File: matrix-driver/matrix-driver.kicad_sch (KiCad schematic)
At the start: 27 parts, among them J1 Conn_01x09, U1 TPS562202, U2 LP5891MRRFR, U3 TPS562202

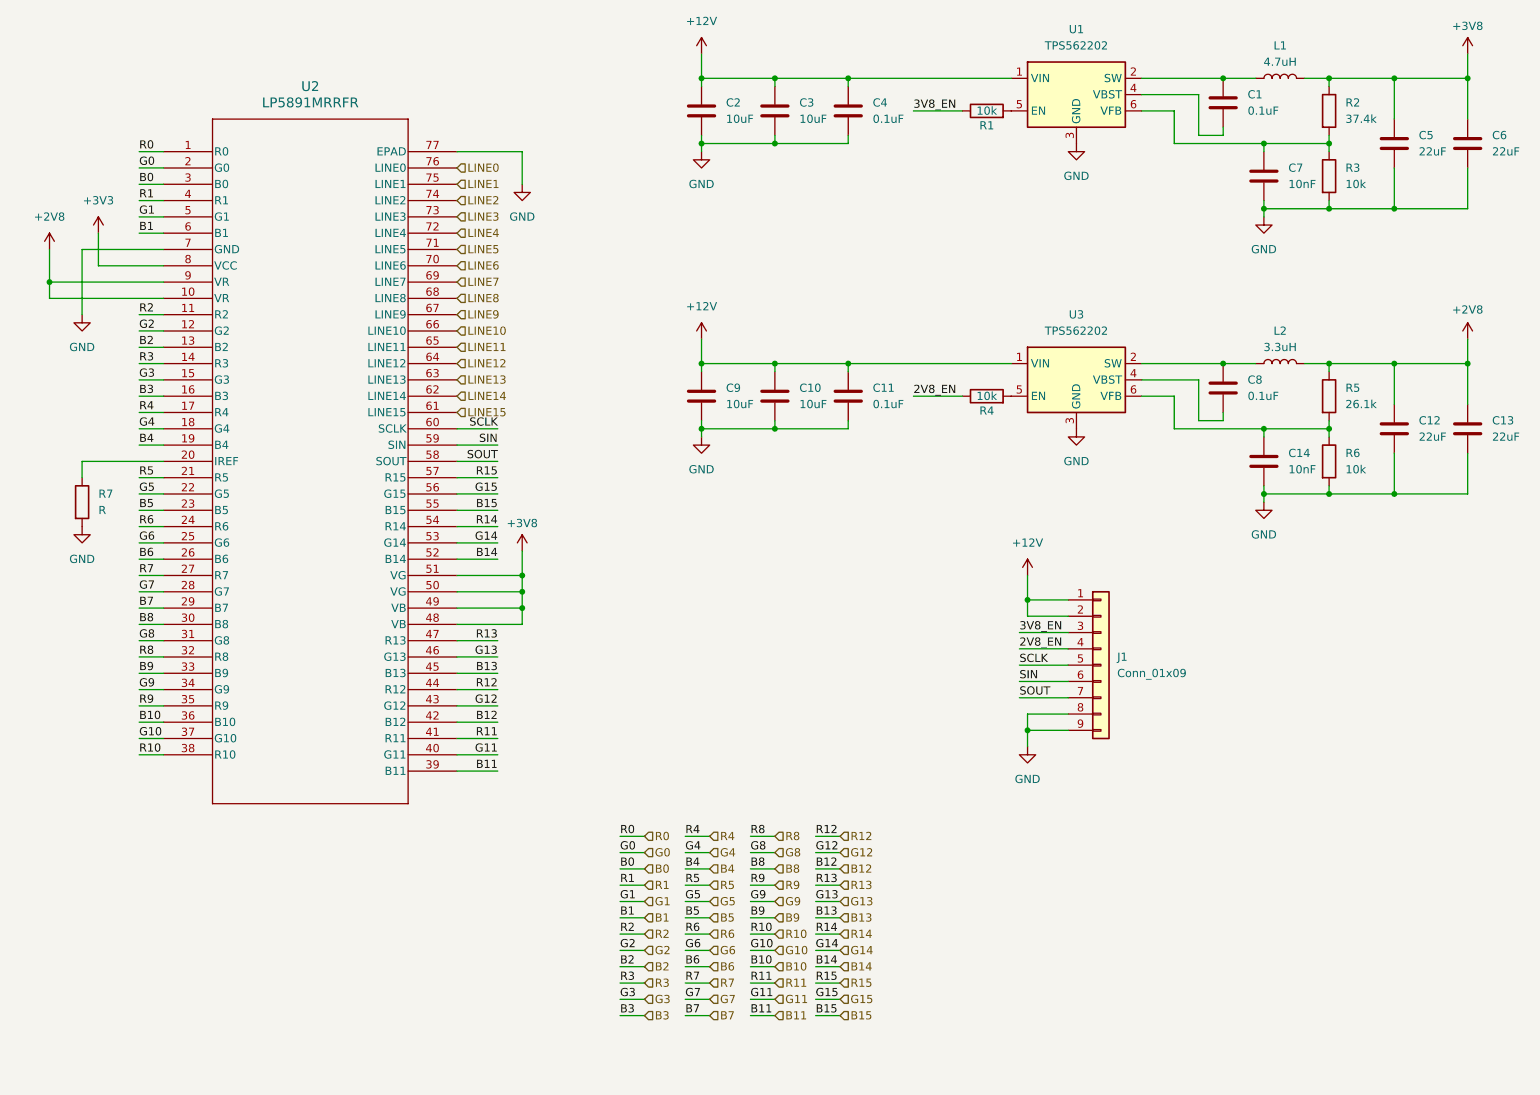
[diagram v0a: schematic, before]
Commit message: laid out proper schematic and connector interface for driver, added new conn libs, todo add correct inductors
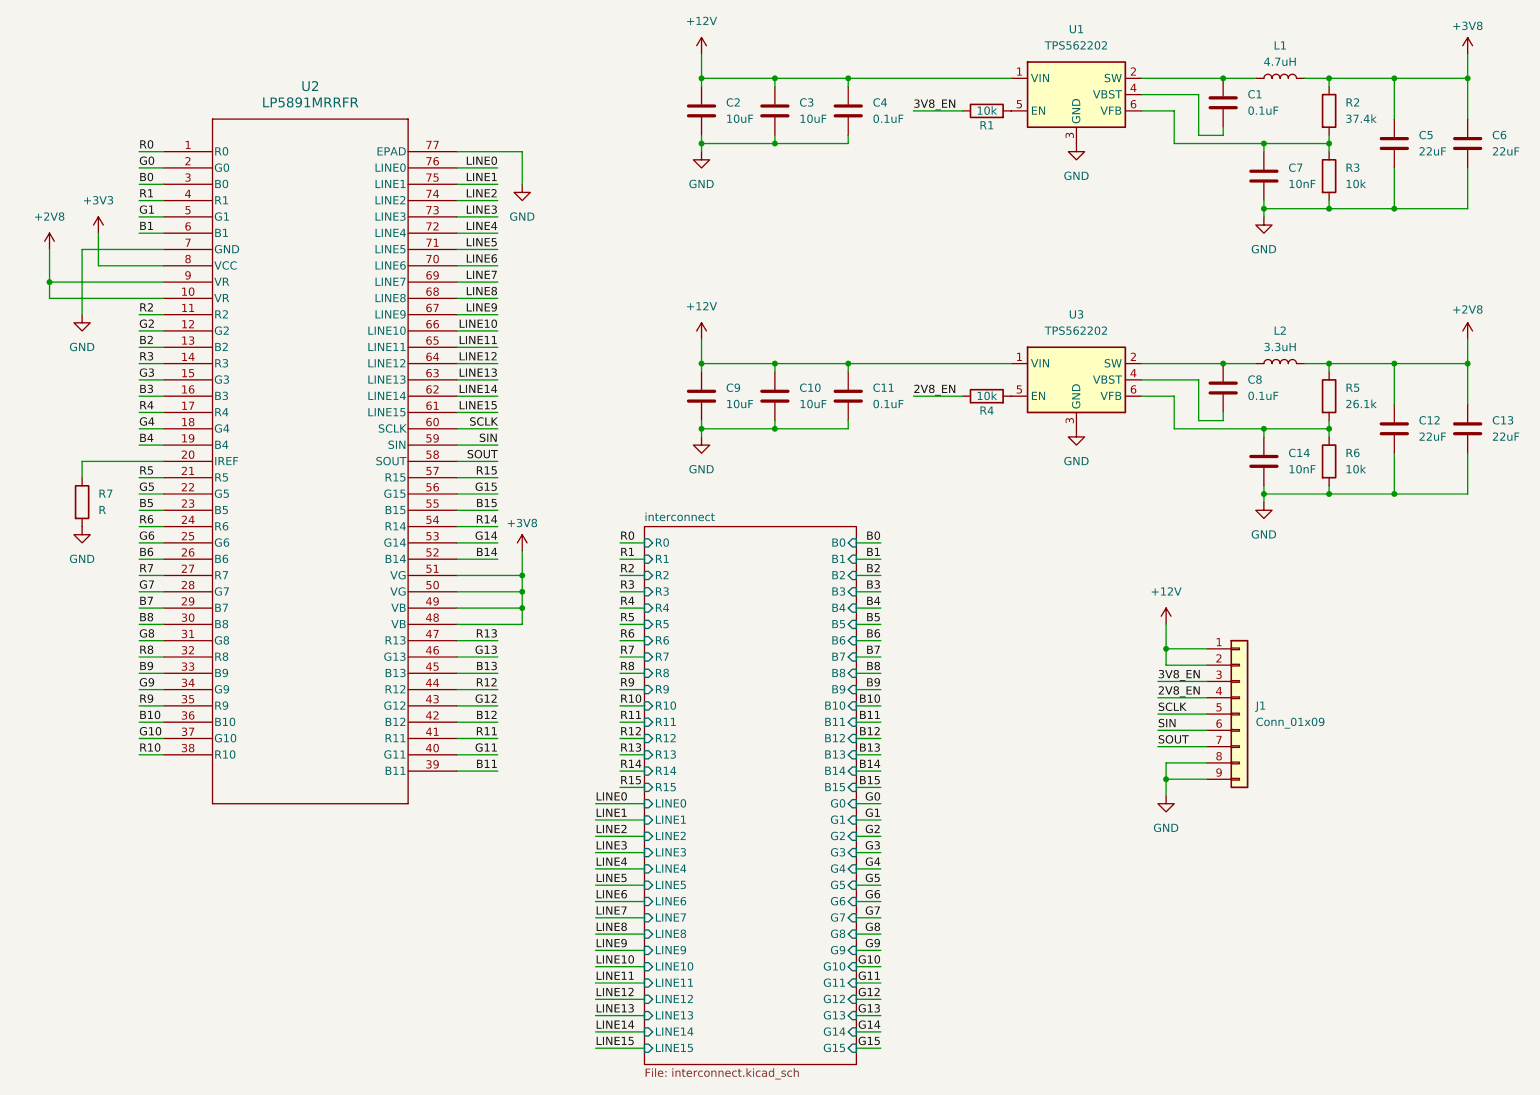
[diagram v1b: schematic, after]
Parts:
- J1: footprint (none) -> CONN_BM09B-XASS-TF_JST:CONN_BM09B-XASS-TF_JST
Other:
- added sheet interconnect (interconnect.kicad_sch)
- moved on the sheet: J1

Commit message: added 3v3 regulator again and added footprints to layout
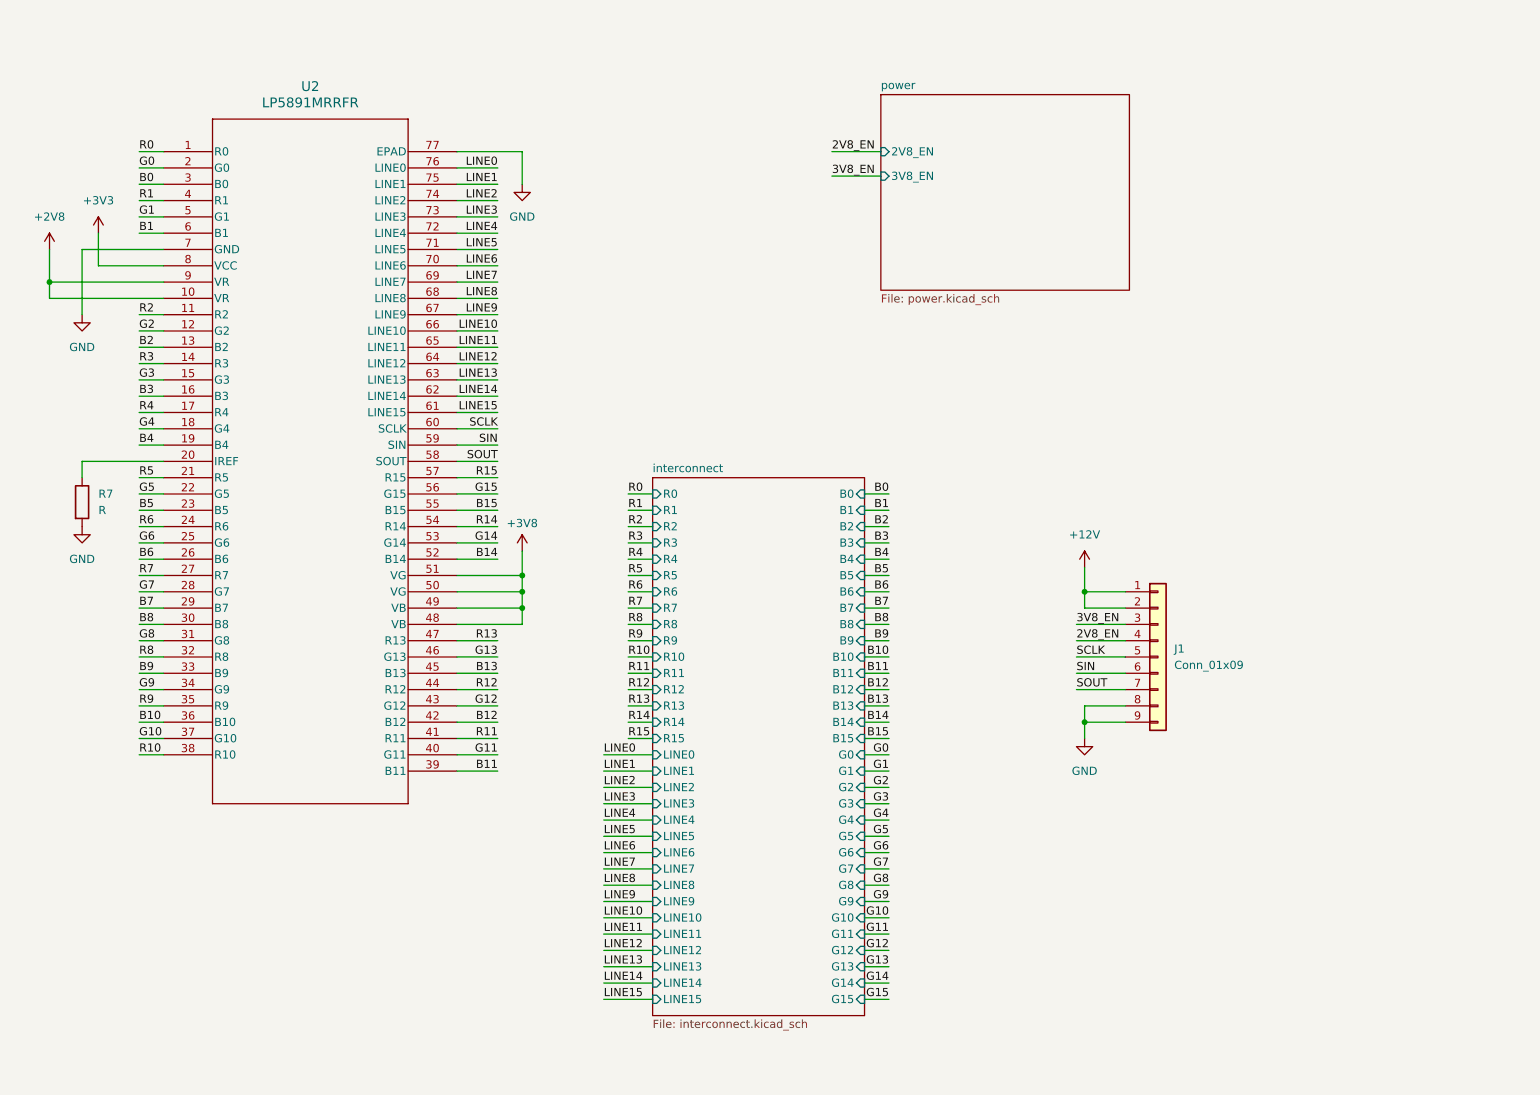
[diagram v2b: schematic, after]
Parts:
- removed C1, C11, C4, C8: 0.1uF, Capacitor_SMD:C_0603_1608Metric, symbol Device:C
- removed C10, C2, C3, C9: 10uF, Capacitor_SMD:C_1206_3216Metric, symbol Device:C
- removed C12, C13, C5, C6: 22uF, Capacitor_SMD:C_1206_3216Metric, symbol Device:C
- removed C14, C7: 10nF, Capacitor_SMD:C_0603_1608Metric, symbol Device:C
- removed L1: 4.7uH, symbol Device:L
- removed L2: 3.3uH, symbol Device:L
- removed R1, R3, R4, R6: 10k, Resistor_SMD:R_0603_1608Metric, symbol Device:R
- removed R2: 37.4k, Resistor_SMD:R_0603_1608Metric, symbol Device:R
- removed R5: 26.1k, Resistor_SMD:R_0603_1608Metric, symbol Device:R
- removed U1, U3: TPS562202, Package_TO_SOT_SMD:SOT-563, symbol Regulator_Switching:TPS562202
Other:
- added sheet power (power.kicad_sch)
- moved on the sheet: J1

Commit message: added gerbers and finalized v1.0
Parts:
- added H1, H2, H3, H4: MountingHole, MountingHole:MountingHole_3.2mm_M3_DIN965, symbol Mechanical:MountingHole
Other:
- moved on the sheet: J1

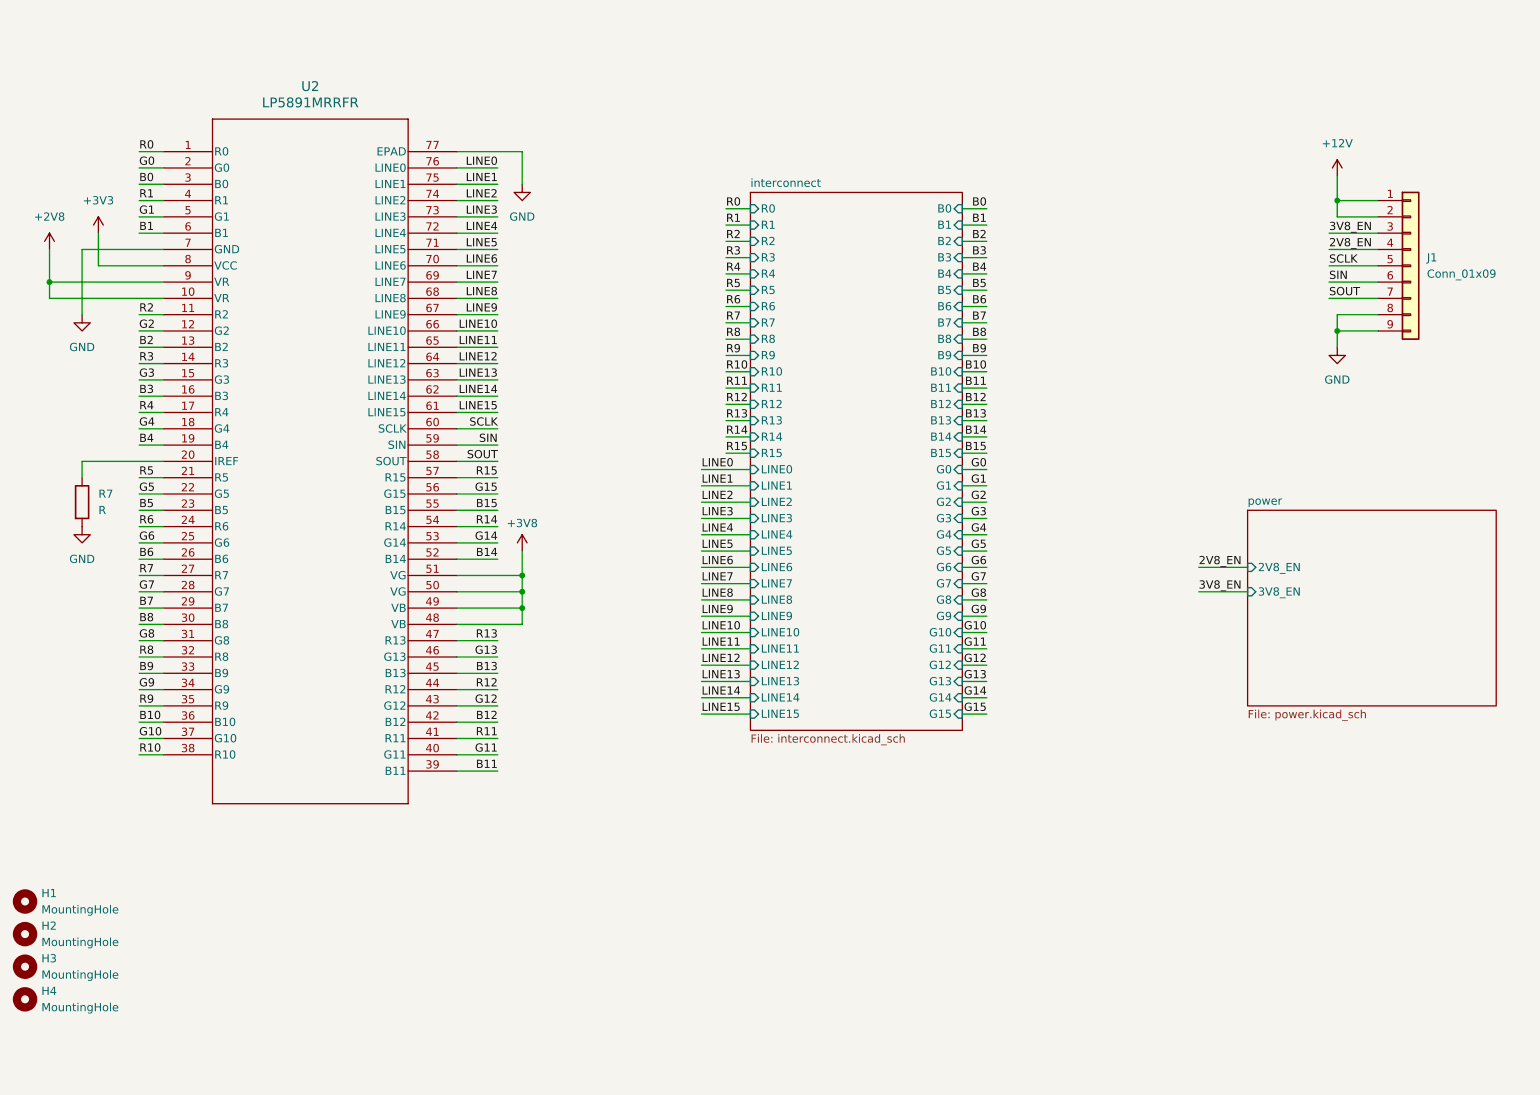
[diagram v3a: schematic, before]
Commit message: changed to through hole connectors for matrix drive unit and updated schematic to reflect thermistors and reserved pin
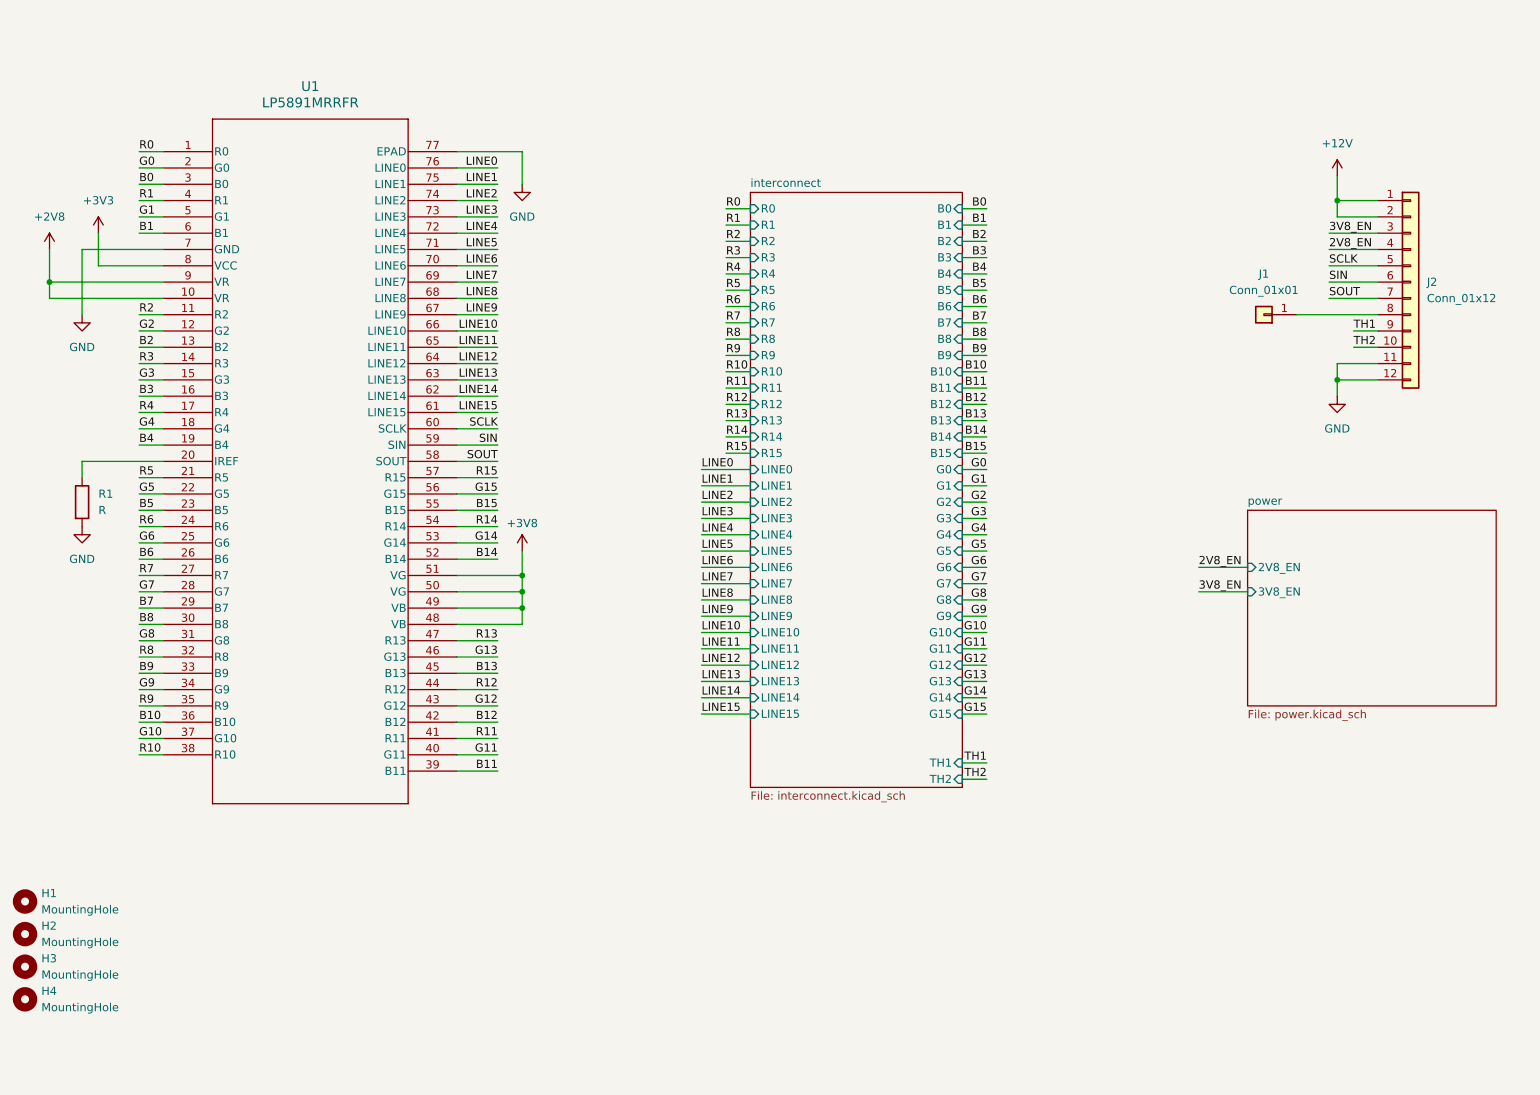
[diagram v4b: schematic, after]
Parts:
- removed J1: Conn_01x09, CONN_BM09B-XASS-TF_JST:CONN_BM09B-XASS-TF_JST, symbol Connector_Generic:Conn_01x09
- added J1: Conn_01x01, Connector_PinHeader_2.54mm:PinHeader_1x01_P2.54mm_Vertical, symbol Connector_Generic:Conn_01x01
- added J2: Conn_01x12, Connector_JST:JST_XA_B12B-XASK-1-A_1x12_P2.50mm_Vertical, symbol Connector_Generic:Conn_01x12
- renumbered R7 to R1, U2 to U1
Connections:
- net +12V: now also J2.1 (Pin_1), J2.2 (Pin_2)
- net 2V8_EN: now also J2.4 (Pin_4)
- net 3V8_EN: now also J2.3 (Pin_3)
- net GND: now also J2.11 (Pin_11), J2.12 (Pin_12)
- net SCLK: now also J2.5 (Pin_5)
- net SIN: now also J2.6 (Pin_6)
- net SOUT: now also J2.7 (Pin_7)
- new net: J1.1 (Pin_1), J2.8 (Pin_8)
- new net TH1: J2.9 (Pin_9)
- new net TH2: J2.10 (Pin_10)
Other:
- sheet interconnect ports: added TH1, TH2; removed none
